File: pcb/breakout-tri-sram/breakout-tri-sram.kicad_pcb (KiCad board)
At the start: 4 copper layers, 100 x 100 mm, 148 parts, among them J101 FX18-120P-0.8SV20, J102 FX18-120S-0.8SV20, U101 IS61WV102416DBLL-10TLI, U102 IS61WV102416DBLL-10TLI, U103 IS61WV102416DBLL-10TLI, U201 74LCX541FT, U202 74LCX541FT, U203 74LCX541FT, U204 74LCX541FT, U205 74LCX541FT, U206 74LCX541FT, U207 74LCX541FT, U208 74LCX541FT, U209 74LCX541FT, U210 74LCX541FT, U211 74LCX541FT, U212 74LCX541FT, U301 74LCX541FT, U302 74LCX541FT, U303 74LCX541FT, U304 74LCX541FT, U305 74LCX541FT, U306 74LCX541FT, U401 74LCX541FT, U402 74LCX541FT, U403 74LCX541FT, U404 74LCX541FT, U405 74LCX541FT, U406 74LCX541FT, U501 74LCX541FT, U502 74LCX541FT, U503 74LCX541FT, U504 74LCX541FT, U505 74LCX541FT, U506 74LCX541FT, U507 74LCX541FT, U508 74LCX541FT, U509 74LCX541FT

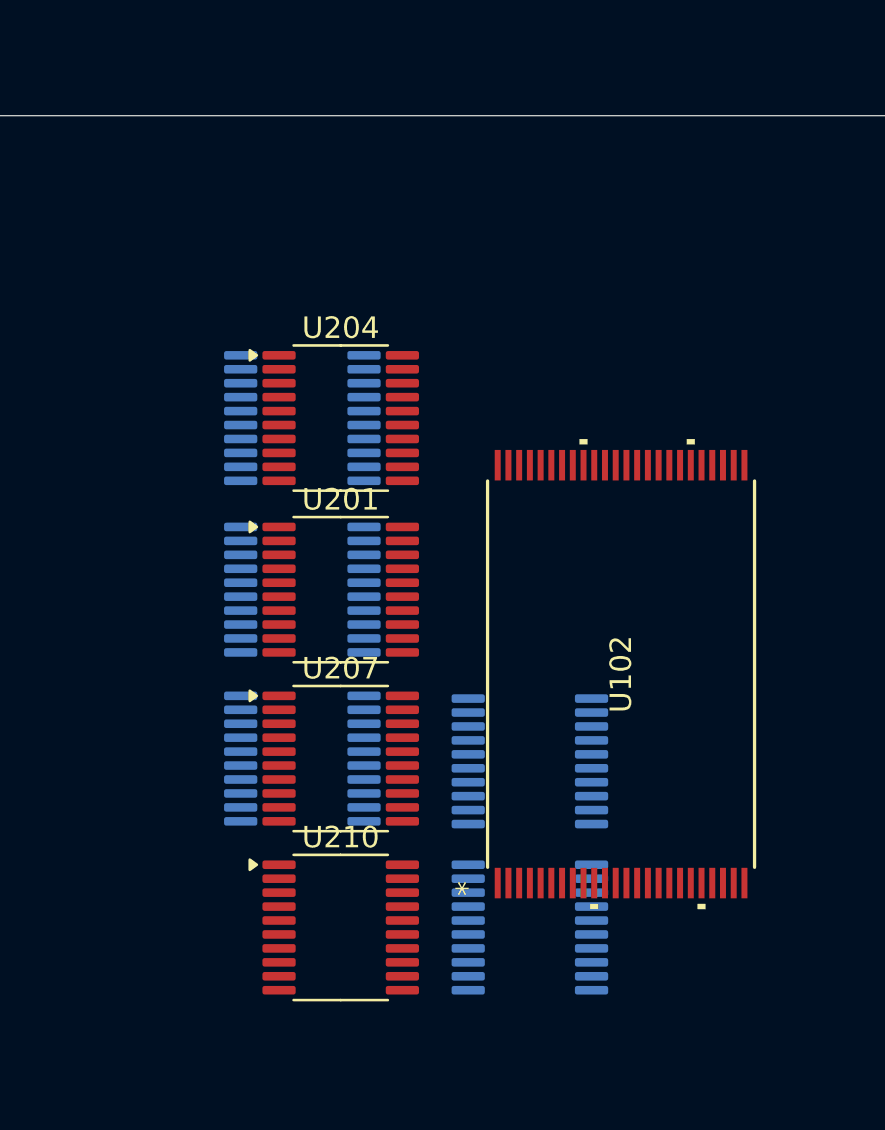
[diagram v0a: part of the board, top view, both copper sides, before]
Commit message: [pci][pci-sram] move to latched buffers
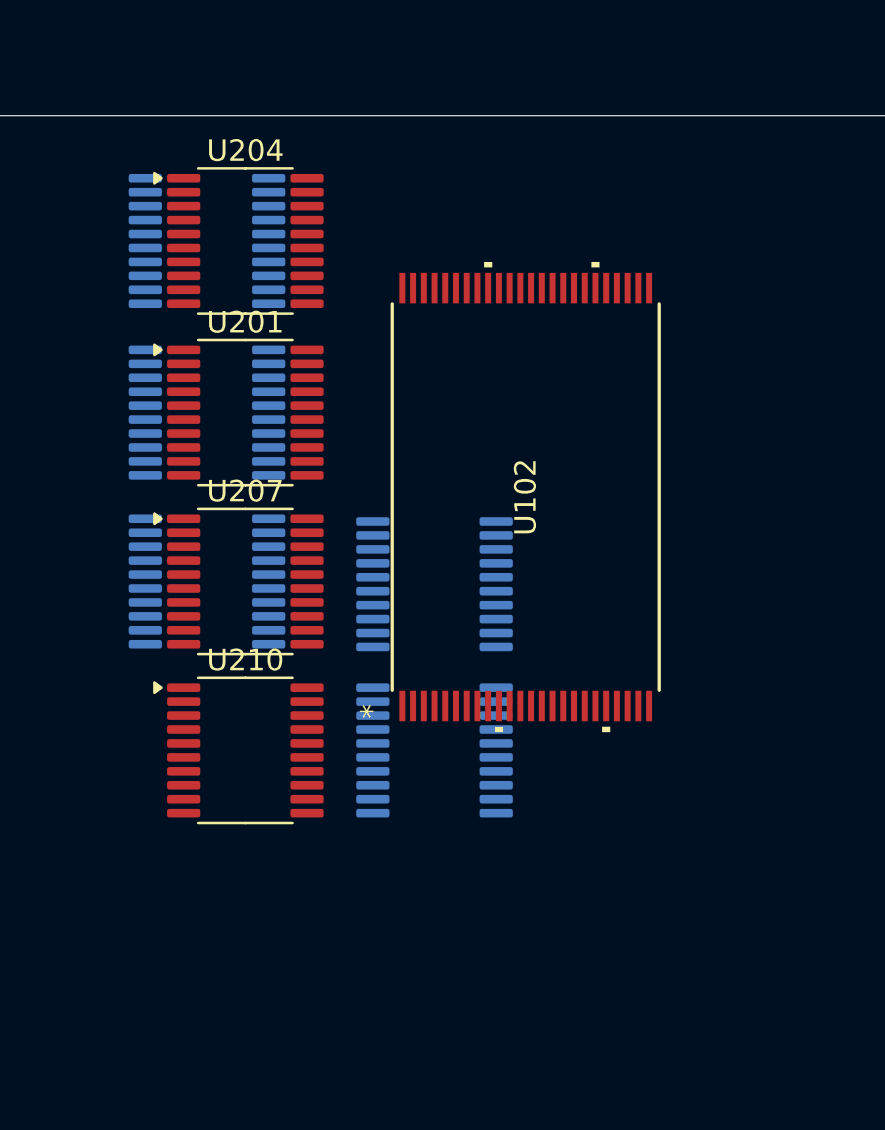
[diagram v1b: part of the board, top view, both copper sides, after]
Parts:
- U201, U202, U203, U204, U205, U206, U207, U208, U209, U210, U211, U212, U301, U302, U303, U304, U305, U306, U401, U402, U403, U404, U405, U406, U501, U502, U503, U504, U505, U506, U507, U508, U509: value 74LCX541FT -> 74LS573
- moved U102 9.38 mm to (53.2, 45.0)
- moved U201 9.38 mm to (40.1, 41.0)
- moved U210 9.38 mm to (40.1, 56.8)
- moved U301 9.38 mm to (49.0, 49.0)
- moved U304 9.38 mm to (49.0, 56.8)
- moved U501 9.38 mm to (38.4, 41.0)
- moved U204 9.38 mm to (40.1, 33.0)
- moved U207 9.38 mm to (40.1, 48.9)
- moved U504 9.38 mm to (38.4, 33.0)
- moved U507 9.38 mm to (38.4, 48.9)
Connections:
- J101 pad 51: unconnected-(J101-Pad51) -> /A2D_L
- J101 pad 52: unconnected-(J101-Pad52) -> /VGA_A_L
- J101 pad 53: unconnected-(J101-Pad53) -> /VGA_D_L
- U201 pad 11: /0_A7 -> /A2D_L
- U201 pad 12: /0_A6 -> /0_A7
- U201 pad 13: /0_A5 -> /0_A6
- U201 pad 14: /0_A4 -> /0_A5
- U201 pad 15: /0_A3 -> /0_A4
- U201 pad 16: /0_A2 -> /0_A3
- U201 pad 17: /0_A1 -> /0_A2
- U201 pad 18: /0_A0 -> /0_A1
- U201 pad 19: /A2D_0_EN# -> /0_A0
- U202 pad 11: /1_A7 -> /A2D_L
- U202 pad 12: /1_A6 -> /1_A7
- U202 pad 13: /1_A5 -> /1_A6
- U202 pad 14: /1_A4 -> /1_A5
- U202 pad 15: /1_A3 -> /1_A4
- U202 pad 16: /1_A2 -> /1_A3
- U202 pad 17: /1_A1 -> /1_A2
- U202 pad 18: /1_A0 -> /1_A1
- U202 pad 19: /A2D_1_EN# -> /1_A0
- U203 pad 11: /2_A7 -> /A2D_L
- U203 pad 12: /2_A6 -> /2_A7
- U203 pad 13: /2_A5 -> /2_A6
- U203 pad 14: /2_A4 -> /2_A5
- U203 pad 15: /2_A3 -> /2_A4
- U203 pad 16: /2_A2 -> /2_A3
- U203 pad 17: /2_A1 -> /2_A2
- U203 pad 18: /2_A0 -> /2_A1
- U203 pad 19: /A2D_2_EN# -> /2_A0
- U204 pad 11: /0_A15 -> /A2D_L
- U204 pad 12: /0_A14 -> /0_A15
- U204 pad 13: /0_A13 -> /0_A14
- U204 pad 14: /0_A12 -> /0_A13
- U204 pad 15: /0_A11 -> /0_A12
- U204 pad 16: /0_A10 -> /0_A11
- U204 pad 17: /0_A9 -> /0_A10
- U204 pad 18: /0_A8 -> /0_A9
- U204 pad 19: /A2D_0_EN# -> /0_A8
- U205 pad 11: /2_A15 -> /A2D_L
- U205 pad 12: /2_A14 -> /2_A15
- U205 pad 13: /2_A13 -> /2_A14
- U205 pad 14: /2_A12 -> /2_A13
- U205 pad 15: /2_A11 -> /2_A12
- U205 pad 16: /2_A10 -> /2_A11
- U205 pad 17: /2_A9 -> /2_A10
- U205 pad 18: /2_A8 -> /2_A9
- U205 pad 19: /A2D_2_EN# -> /2_A8
- U206 pad 11: /1_A15 -> /A2D_L
- U206 pad 12: /1_A14 -> /1_A15
- U206 pad 13: /1_A13 -> /1_A14
- U206 pad 14: /1_A12 -> /1_A13
- U206 pad 15: /1_A11 -> /1_A12
- U206 pad 16: /1_A10 -> /1_A11
- U206 pad 17: /1_A9 -> /1_A10
- U206 pad 18: /1_A8 -> /1_A9
- U206 pad 19: /A2D_1_EN# -> /1_A8
- U207 pad 11: /0_D3 -> /A2D_L
- U207 pad 12: /0_D2 -> /0_D3
- U207 pad 13: /0_D1 -> /0_D2
- U207 pad 14: /0_D0 -> /0_D1
- U207 pad 15: /0_A19 -> /0_D0
- U207 pad 16: /0_A18 -> /0_A19
- U207 pad 17: /0_A17 -> /0_A18
- U207 pad 18: /0_A16 -> /0_A17
- U207 pad 19: /A2D_0_EN# -> /0_A16
- U208 pad 11: /2_D3 -> /A2D_L
- U208 pad 12: /2_D2 -> /2_D3
- U208 pad 13: /2_D1 -> /2_D2
- U208 pad 14: /2_D0 -> /2_D1
- U208 pad 15: /2_A19 -> /2_D0
- U208 pad 16: /2_A18 -> /2_A19
- U208 pad 17: /2_A17 -> /2_A18
- U208 pad 18: /2_A16 -> /2_A17
- U208 pad 19: /A2D_2_EN# -> /2_A16
- U209 pad 11: /1_D3 -> /A2D_L
- U209 pad 12: /1_D2 -> /1_D3
- U209 pad 13: /1_D1 -> /1_D2
- U209 pad 14: /1_D0 -> /1_D1
- U209 pad 15: /1_A19 -> /1_D0
- U209 pad 16: /1_A18 -> /1_A19
- U209 pad 17: /1_A17 -> /1_A18
- U209 pad 18: /1_A16 -> /1_A17
- U209 pad 19: /A2D_1_EN# -> /1_A16
- U210 pad 11: /0_D11 -> /A2D_L
- U210 pad 12: /0_D10 -> /0_D11
- U210 pad 13: /0_D9 -> /0_D10
- U210 pad 14: /0_D8 -> /0_D9
- U210 pad 15: /0_D7 -> /0_D8
- U210 pad 16: /0_D6 -> /0_D7
- U210 pad 17: /0_D5 -> /0_D6
- U210 pad 18: /0_D4 -> /0_D5
- U210 pad 19: /A2D_0_EN# -> /0_D4
- U211 pad 11: /2_D11 -> /A2D_L
- U211 pad 12: /2_D10 -> /2_D11
- U211 pad 13: /2_D9 -> /2_D10
- U211 pad 14: /2_D8 -> /2_D9
- U211 pad 15: /2_D7 -> /2_D8
- U211 pad 16: /2_D6 -> /2_D7
- U211 pad 17: /2_D5 -> /2_D6
- U211 pad 18: /2_D4 -> /2_D5
- U211 pad 19: /A2D_2_EN# -> /2_D4
- U212 pad 11: /1_D11 -> /A2D_L
- U212 pad 12: /1_D10 -> /1_D11
- U212 pad 13: /1_D9 -> /1_D10
- U212 pad 14: /1_D8 -> /1_D9
- U212 pad 15: /1_D7 -> /1_D8
- U212 pad 16: /1_D6 -> /1_D7
- U212 pad 17: /1_D5 -> /1_D6
- U212 pad 18: /1_D4 -> /1_D5
- U212 pad 19: /A2D_1_EN# -> /1_D4
- U301 pad 11: /0_D3 -> +3V3
- U301 pad 12: /0_D2 -> /0_D3
- U301 pad 13: /0_D1 -> /0_D2
- U301 pad 14: /0_D0 -> /0_D1
- U301 pad 15: unconnected-(U301-Y3-Pad15) -> /0_D0
- U301 pad 19: /BLK_0_EN# -> unconnected-(U301-Q0-Pad19)
- U302 pad 11: /1_D3 -> +3V3
- U302 pad 12: /1_D2 -> /1_D3
- U302 pad 13: /1_D1 -> /1_D2
- U302 pad 14: /1_D0 -> /1_D1
- U302 pad 15: unconnected-(U302-Y3-Pad15) -> /1_D0
- U302 pad 19: /BLK_2_EN# -> unconnected-(U302-Q0-Pad19)
- U303 pad 11: /1_D3 -> +3V3
- U303 pad 12: /1_D2 -> /1_D3
- U303 pad 13: /1_D1 -> /1_D2
- U303 pad 14: /1_D0 -> /1_D1
- U303 pad 15: unconnected-(U303-Y3-Pad15) -> /1_D0
- U303 pad 19: /BLK_1_EN# -> unconnected-(U303-Q0-Pad19)
- U304 pad 11: /0_D11 -> +3V3
- U304 pad 12: /0_D10 -> /0_D11
- U304 pad 13: /0_D9 -> /0_D10
- U304 pad 14: /0_D8 -> /0_D9
- U304 pad 15: /0_D7 -> /0_D8
- U304 pad 16: /0_D6 -> /0_D7
- U304 pad 17: /0_D5 -> /0_D6
- U304 pad 18: /0_D4 -> /0_D5
- U304 pad 19: /BLK_0_EN# -> /0_D4
- U305 pad 11: /1_D11 -> +3V3
- U305 pad 12: /1_D10 -> /1_D11
- U305 pad 13: /1_D9 -> /1_D10
- U305 pad 14: /1_D8 -> /1_D9
- U305 pad 15: /1_D7 -> /1_D8
- U305 pad 16: /1_D6 -> /1_D7
- U305 pad 17: /1_D5 -> /1_D6
- U305 pad 18: /1_D4 -> /1_D5
- U305 pad 19: /BLK_2_EN# -> /1_D4
- U306 pad 11: /1_D11 -> +3V3
- U306 pad 12: /1_D10 -> /1_D11
- U306 pad 13: /1_D9 -> /1_D10
- U306 pad 14: /1_D8 -> /1_D9
- U306 pad 15: /1_D7 -> /1_D8
- U306 pad 16: /1_D6 -> /1_D7
- U306 pad 17: /1_D5 -> /1_D6
- U306 pad 18: /1_D4 -> /1_D5
- U306 pad 19: /BLK_1_EN# -> /1_D4
- U401 pad 11: /VGA_B_3 -> /VGA_D_L
- U401 pad 12: /VGA_B_2 -> /VGA_B_3
- U401 pad 13: /VGA_B_1 -> /VGA_B_2
- U401 pad 14: /VGA_B_0 -> /VGA_B_1
- U401 pad 15: unconnected-(U401-Y3-Pad15) -> /VGA_B_0
- U401 pad 17: /VGA_VSYNC -> unconnected-(U401-Q2-Pad17)
- U401 pad 18: /VGA_HSYNC -> /VGA_VSYNC
- U401 pad 19: /VGA_0_D_EN# -> /VGA_HSYNC
- U402 pad 11: /VGA_B_3 -> /VGA_D_L
- U402 pad 12: /VGA_B_2 -> /VGA_B_3
- U402 pad 13: /VGA_B_1 -> /VGA_B_2
- U402 pad 14: /VGA_B_0 -> /VGA_B_1
- U402 pad 15: unconnected-(U402-Y3-Pad15) -> /VGA_B_0
- U402 pad 17: /VGA_VSYNC -> unconnected-(U402-Q2-Pad17)
- U402 pad 18: /VGA_HSYNC -> /VGA_VSYNC
- U402 pad 19: /VGA_2_D_EN# -> /VGA_HSYNC
- U403 pad 11: /VGA_B_3 -> /VGA_D_L
- U403 pad 12: /VGA_B_2 -> /VGA_B_3
- U403 pad 13: /VGA_B_1 -> /VGA_B_2
- U403 pad 14: /VGA_B_0 -> /VGA_B_1
- U403 pad 15: unconnected-(U403-Y3-Pad15) -> /VGA_B_0
- U403 pad 17: /VGA_VSYNC -> unconnected-(U403-Q2-Pad17)
- U403 pad 18: /VGA_HSYNC -> /VGA_VSYNC
- U403 pad 19: /VGA_1_D_EN# -> /VGA_HSYNC
- U404 pad 11: /VGA_R_3 -> /VGA_D_L
- U404 pad 12: /VGA_R_2 -> /VGA_R_3
- U404 pad 13: /VGA_R_1 -> /VGA_R_2
- U404 pad 14: /VGA_R_0 -> /VGA_R_1
- U404 pad 15: /VGA_G_3 -> /VGA_R_0
- U404 pad 16: /VGA_G_2 -> /VGA_G_3
- U404 pad 17: /VGA_G_1 -> /VGA_G_2
- U404 pad 18: /VGA_G_0 -> /VGA_G_1
- U404 pad 19: /VGA_0_D_EN# -> /VGA_G_0
- U405 pad 11: /VGA_R_3 -> /VGA_D_L
- U405 pad 12: /VGA_R_2 -> /VGA_R_3
- U405 pad 13: /VGA_R_1 -> /VGA_R_2
- U405 pad 14: /VGA_R_0 -> /VGA_R_1
- U405 pad 15: /VGA_G_3 -> /VGA_R_0
- U405 pad 16: /VGA_G_2 -> /VGA_G_3
- U405 pad 17: /VGA_G_1 -> /VGA_G_2
- U405 pad 18: /VGA_G_0 -> /VGA_G_1
- U405 pad 19: /VGA_2_D_EN# -> /VGA_G_0
- U406 pad 11: /VGA_R_3 -> /VGA_D_L
- U406 pad 12: /VGA_R_2 -> /VGA_R_3
- U406 pad 13: /VGA_R_1 -> /VGA_R_2
- U406 pad 14: /VGA_R_0 -> /VGA_R_1
- U406 pad 15: /VGA_G_3 -> /VGA_R_0
- U406 pad 16: /VGA_G_2 -> /VGA_G_3
- U406 pad 17: /VGA_G_1 -> /VGA_G_2
- U406 pad 18: /VGA_G_0 -> /VGA_G_1
- U406 pad 19: /VGA_1_D_EN# -> /VGA_G_0
- U501 pad 11: /0_A7 -> /VGA_A_L
- U501 pad 12: /0_A6 -> /0_A7
- U501 pad 13: /0_A5 -> /0_A6
- U501 pad 14: /0_A4 -> /0_A5
- U501 pad 15: /0_A3 -> /0_A4
- U501 pad 16: /0_A2 -> /0_A3
- U501 pad 17: /0_A1 -> /0_A2
- U501 pad 18: /0_A0 -> /0_A1
- U501 pad 19: /VGA_0_A_EN# -> /0_A0
- U502 pad 11: /1_A7 -> /VGA_A_L
- U502 pad 12: /1_A6 -> /1_A7
- U502 pad 13: /1_A5 -> /1_A6
- U502 pad 14: /1_A4 -> /1_A5
- U502 pad 15: /1_A3 -> /1_A4
- U502 pad 16: /1_A2 -> /1_A3
- U502 pad 17: /1_A1 -> /1_A2
- U502 pad 18: /1_A0 -> /1_A1
- U502 pad 19: /VGA_1_A_EN# -> /1_A0
- U503 pad 11: /2_A7 -> /VGA_A_L
- U503 pad 12: /2_A6 -> /2_A7
- U503 pad 13: /2_A5 -> /2_A6
- U503 pad 14: /2_A4 -> /2_A5
- U503 pad 15: /2_A3 -> /2_A4
- U503 pad 16: /2_A2 -> /2_A3
- U503 pad 17: /2_A1 -> /2_A2
- U503 pad 18: /2_A0 -> /2_A1
- U503 pad 19: /VGA_2_A_EN# -> /2_A0
- U504 pad 11: /0_A15 -> /VGA_A_L
- U504 pad 12: /0_A14 -> /0_A15
- U504 pad 13: /0_A13 -> /0_A14
- U504 pad 14: /0_A12 -> /0_A13
- U504 pad 15: /0_A11 -> /0_A12
- U504 pad 16: /0_A10 -> /0_A11
- U504 pad 17: /0_A9 -> /0_A10
- U504 pad 18: /0_A8 -> /0_A9
- U504 pad 19: /VGA_0_A_EN# -> /0_A8
- U505 pad 11: /2_A15 -> /VGA_A_L
- U505 pad 12: /2_A14 -> /2_A15
- U505 pad 13: /2_A13 -> /2_A14
- U505 pad 14: /2_A12 -> /2_A13
- U505 pad 15: /2_A11 -> /2_A12
- U505 pad 16: /2_A10 -> /2_A11
- U505 pad 17: /2_A9 -> /2_A10
- U505 pad 18: /2_A8 -> /2_A9
- U505 pad 19: /VGA_2_A_EN# -> /2_A8
- U506 pad 11: /1_A15 -> /VGA_A_L
- U506 pad 12: /1_A14 -> /1_A15
- U506 pad 13: /1_A13 -> /1_A14
- U506 pad 14: /1_A12 -> /1_A13
- U506 pad 15: /1_A11 -> /1_A12
- U506 pad 16: /1_A10 -> /1_A11
- U506 pad 17: /1_A9 -> /1_A10
- U506 pad 18: /1_A8 -> /1_A9
- U506 pad 19: /VGA_1_A_EN# -> /1_A8
- U507 pad 11: unconnected-(U507-Y7-Pad11) -> /VGA_A_L
- U507 pad 15: /0_A19 -> unconnected-(U507-Q4-Pad15)
- U507 pad 16: /0_A18 -> /0_A19
- U507 pad 17: /0_A17 -> /0_A18
- U507 pad 18: /0_A16 -> /0_A17
- U507 pad 19: /VGA_0_A_EN# -> /0_A16
- U508 pad 11: unconnected-(U508-Y7-Pad11) -> /VGA_A_L
- U508 pad 15: /2_A19 -> unconnected-(U508-Q4-Pad15)
- U508 pad 16: /2_A18 -> /2_A19
- U508 pad 17: /2_A17 -> /2_A18
- U508 pad 18: /2_A16 -> /2_A17
- U508 pad 19: /VGA_2_A_EN# -> /2_A16
- U509 pad 11: unconnected-(U509-Y7-Pad11) -> /VGA_A_L
- U509 pad 15: /1_A19 -> unconnected-(U509-Q4-Pad15)
- U509 pad 16: /1_A18 -> /1_A19
- U509 pad 17: /1_A17 -> /1_A18
- U509 pad 18: /1_A16 -> /1_A17
- U509 pad 19: /VGA_1_A_EN# -> /1_A16

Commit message: [pcb][tri-sram] 3xsram routed
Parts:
- removed C202, C205, C208, C211, C214, C217, C220, C223, C226, C229, C232, C235, C302, C305, C308, C311, C314, C317, C402, C405, C408, C411, C414, C502, C505, C508, C511, C514, C517, C520, C523, C526: 0.1uf, Capacitor_SMD:C_0402_1005Metric
- removed C210, C213, C216, C219, C222, C225, C228, C231, C234, C301, C304, C307, C310, C313, C316, C401, C404, C407, C416, C501, C504, C507, C510, C513, C516: 22uf, Capacitor_SMD:C_0603_1608Metric
- C303, C306, C309, C312, C315, C318, C403, C406, C409, C410, C412, C413, C415, C417, C418, C503, C506, C509, C512, C515, C518, C519, C521, C522, C524, C525, C527, U302, U303, U305, U306, U401, U402, U403, U404, U405, U406, U502, U503, U505, U506, U508, U509: moved to B.Cu
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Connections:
- U201 pad 12: /0_A7 -> /0_A0
- U201 pad 13: /0_A6 -> /0_A19
- U201 pad 14: /0_A5 -> /0_A18
- U201 pad 15: /0_A4 -> /0_A17
- U201 pad 16: /0_A3 -> /0_A16
- U201 pad 17: /0_A2 -> /0_A15
- U201 pad 18: /0_A1 -> /0_A6
- U201 pad 19: /0_A0 -> /0_A5
- U201 pad 2: /A2D_X_0 -> /A2D_X_5
- U201 pad 3: /A2D_X_1 -> /A2D_X_6
- U201 pad 4: /A2D_X_2 -> /A2D_Y_5
- U201 pad 5: /A2D_X_3 -> /A2D_Y_6
- U201 pad 6: /A2D_X_4 -> /A2D_Y_7
- U201 pad 7: /A2D_X_5 -> /A2D_Y_8
- U201 pad 8: /A2D_X_6 -> /A2D_Y_9
- U201 pad 9: /A2D_X_7 -> /A2D_X_0
- U202 pad 12: /1_A7 -> /1_A0
- U202 pad 13: /1_A6 -> /1_A19
- U202 pad 14: /1_A5 -> /1_A18
- U202 pad 15: /1_A4 -> /1_A17
- U202 pad 16: /1_A3 -> /1_A16
- U202 pad 17: /1_A2 -> /1_A15
- U202 pad 18: /1_A1 -> /1_A6
- U202 pad 19: /1_A0 -> /1_A5
- U202 pad 2: /A2D_X_0 -> /A2D_X_5
- U202 pad 3: /A2D_X_1 -> /A2D_X_6
- U202 pad 4: /A2D_X_2 -> /A2D_Y_5
- U202 pad 5: /A2D_X_3 -> /A2D_Y_6
- U202 pad 6: /A2D_X_4 -> /A2D_Y_7
- U202 pad 7: /A2D_X_5 -> /A2D_Y_8
- U202 pad 8: /A2D_X_6 -> /A2D_Y_9
- U202 pad 9: /A2D_X_7 -> /A2D_X_0
- U203 pad 12: /2_A7 -> /2_A0
- U203 pad 13: /2_A6 -> /2_A19
- U203 pad 14: /2_A5 -> /2_A18
- U203 pad 15: /2_A4 -> /2_A17
- U203 pad 16: /2_A3 -> /2_A16
- U203 pad 17: /2_A2 -> /2_A15
- U203 pad 18: /2_A1 -> /2_A6
- U203 pad 19: /2_A0 -> /2_A5
- U203 pad 2: /A2D_X_0 -> /A2D_X_5
- U203 pad 3: /A2D_X_1 -> /A2D_X_6
- U203 pad 4: /A2D_X_2 -> /A2D_Y_5
- U203 pad 5: /A2D_X_3 -> /A2D_Y_6
- U203 pad 6: /A2D_X_4 -> /A2D_Y_7
- U203 pad 7: /A2D_X_5 -> /A2D_Y_8
- U203 pad 8: /A2D_X_6 -> /A2D_Y_9
- U203 pad 9: /A2D_X_7 -> /A2D_X_0
- U204 pad 12: /0_A15 -> /0_A7
- U204 pad 13: /0_A14 -> /0_A8
- U204 pad 14: /0_A13 -> /0_A9
- U204 pad 15: /0_A12 -> /0_A10
- U204 pad 17: /0_A10 -> /0_A12
- U204 pad 18: /0_A9 -> /0_A13
- U204 pad 19: /0_A8 -> /0_A14
- U204 pad 2: /A2D_X_8 -> /A2D_Y_4
- U204 pad 3: /A2D_X_9 -> /A2D_Y_3
- U204 pad 4: /A2D_Y_0 -> /A2D_Y_2
- U204 pad 6: /A2D_Y_2 -> /A2D_Y_0
- U204 pad 7: /A2D_Y_3 -> /A2D_X_9
- U204 pad 8: /A2D_Y_4 -> /A2D_X_8
- U204 pad 9: /A2D_Y_5 -> /A2D_X_7
- U205 pad 12: /2_A15 -> /2_A7
- U205 pad 13: /2_A14 -> /2_A8
- U205 pad 14: /2_A13 -> /2_A9
- U205 pad 15: /2_A12 -> /2_A10
- U205 pad 17: /2_A10 -> /2_A12
- U205 pad 18: /2_A9 -> /2_A13
- U205 pad 19: /2_A8 -> /2_A14
- U205 pad 2: /A2D_X_8 -> /A2D_Y_4
- U205 pad 3: /A2D_X_9 -> /A2D_Y_3
- U205 pad 4: /A2D_Y_0 -> /A2D_Y_2
- U205 pad 6: /A2D_Y_2 -> /A2D_Y_0
- U205 pad 7: /A2D_Y_3 -> /A2D_X_9
- U205 pad 8: /A2D_Y_4 -> /A2D_X_8
- U205 pad 9: /A2D_Y_5 -> /A2D_X_7
- U206 pad 12: /1_A15 -> /1_A7
- U206 pad 13: /1_A14 -> /1_A8
- U206 pad 14: /1_A13 -> /1_A9
- U206 pad 15: /1_A12 -> /1_A10
- U206 pad 17: /1_A10 -> /1_A12
- U206 pad 18: /1_A9 -> /1_A13
- U206 pad 19: /1_A8 -> /1_A14
- U206 pad 2: /A2D_X_8 -> /A2D_Y_4
- U206 pad 3: /A2D_X_9 -> /A2D_Y_3
- U206 pad 4: /A2D_Y_0 -> /A2D_Y_2
- U206 pad 6: /A2D_Y_2 -> /A2D_Y_0
- U206 pad 7: /A2D_Y_3 -> /A2D_X_9
- U206 pad 8: /A2D_Y_4 -> /A2D_X_8
- U206 pad 9: /A2D_Y_5 -> /A2D_X_7
- U207 pad 12: /0_D3 -> /0_D0
- U207 pad 13: /0_D2 -> /0_D1
- U207 pad 14: /0_D1 -> /0_D2
- U207 pad 15: /0_D0 -> /0_D3
- U207 pad 16: /0_A19 -> /0_A4
- U207 pad 17: /0_A18 -> /0_A3
- U207 pad 18: /0_A17 -> /0_A2
- U207 pad 19: /0_A16 -> /0_A1
- U207 pad 2: /A2D_Y_6 -> /A2D_X_1
- U207 pad 3: /A2D_Y_7 -> /A2D_X_2
- U207 pad 4: /A2D_Y_8 -> /A2D_X_3
- U207 pad 5: /A2D_Y_9 -> /A2D_X_4
- U207 pad 6: /A2D_B_0 -> /A2D_B_3
- U207 pad 7: /A2D_B_1 -> /A2D_B_2
- U207 pad 8: /A2D_B_2 -> /A2D_B_1
- U207 pad 9: /A2D_B_3 -> /A2D_B_0
- U208 pad 12: /2_D3 -> /2_D0
- U208 pad 13: /2_D2 -> /2_D1
- U208 pad 14: /2_D1 -> /2_D2
- U208 pad 15: /2_D0 -> /2_D3
- U208 pad 16: /2_A19 -> /2_A4
- U208 pad 17: /2_A18 -> /2_A3
- U208 pad 18: /2_A17 -> /2_A2
- U208 pad 19: /2_A16 -> /2_A1
- U208 pad 2: /A2D_Y_6 -> /A2D_X_1
- U208 pad 3: /A2D_Y_7 -> /A2D_X_2
- U208 pad 4: /A2D_Y_8 -> /A2D_X_3
- U208 pad 5: /A2D_Y_9 -> /A2D_X_4
- U208 pad 6: /A2D_B_0 -> /A2D_B_3
- U208 pad 7: /A2D_B_1 -> /A2D_B_2
- U208 pad 8: /A2D_B_2 -> /A2D_B_1
- U208 pad 9: /A2D_B_3 -> /A2D_B_0
- U209 pad 12: /1_D3 -> /1_D0
- U209 pad 13: /1_D2 -> /1_D1
- U209 pad 14: /1_D1 -> /1_D2
- U209 pad 15: /1_D0 -> /1_D3
- U209 pad 16: /1_A19 -> /1_A4
- U209 pad 17: /1_A18 -> /1_A3
- U209 pad 18: /1_A17 -> /1_A2
- U209 pad 19: /1_A16 -> /1_A1
- U209 pad 2: /A2D_Y_6 -> /A2D_X_1
- U209 pad 3: /A2D_Y_7 -> /A2D_X_2
- U209 pad 4: /A2D_Y_8 -> /A2D_X_3
- U209 pad 5: /A2D_Y_9 -> /A2D_X_4
- U209 pad 6: /A2D_B_0 -> /A2D_B_3
- U209 pad 7: /A2D_B_1 -> /A2D_B_2
- U209 pad 8: /A2D_B_2 -> /A2D_B_1
- U209 pad 9: /A2D_B_3 -> /A2D_B_0
- U210 pad 12: /0_D11 -> /0_D8
- U210 pad 13: /0_D10 -> /0_D9
- U210 pad 14: /0_D9 -> /0_D10
- U210 pad 15: /0_D8 -> /0_D11
- U210 pad 6: /A2D_R_0 -> /A2D_R_3
- U210 pad 7: /A2D_R_1 -> /A2D_R_2
- U210 pad 8: /A2D_R_2 -> /A2D_R_1
- U210 pad 9: /A2D_R_3 -> /A2D_R_0
- U211 pad 12: /2_D11 -> /2_D8
- U211 pad 13: /2_D10 -> /2_D9
- U211 pad 14: /2_D9 -> /2_D10
- U211 pad 15: /2_D8 -> /2_D11
- U211 pad 6: /A2D_R_0 -> /A2D_R_3
- U211 pad 7: /A2D_R_1 -> /A2D_R_2
- U211 pad 8: /A2D_R_2 -> /A2D_R_1
- U211 pad 9: /A2D_R_3 -> /A2D_R_0
- U212 pad 12: /1_D11 -> /1_D8
- U212 pad 13: /1_D10 -> /1_D9
- U212 pad 14: /1_D9 -> /1_D10
- U212 pad 15: /1_D8 -> /1_D11
- U212 pad 6: /A2D_R_0 -> /A2D_R_3
- U212 pad 7: /A2D_R_1 -> /A2D_R_2
- U212 pad 8: /A2D_R_2 -> /A2D_R_1
- U212 pad 9: /A2D_R_3 -> /A2D_R_0
- U301 pad 12: /0_D3 -> /0_D0
- U301 pad 13: /0_D2 -> /0_D1
- U301 pad 14: /0_D1 -> /0_D2
- U301 pad 15: /0_D0 -> /0_D3
- U302 pad 12: /1_D3 -> /2_D0
- U302 pad 13: /1_D2 -> /2_D1
- U302 pad 14: /1_D1 -> /2_D2
- U302 pad 15: /1_D0 -> /2_D3
- U303 pad 12: /1_D3 -> /1_D0
- U303 pad 13: /1_D2 -> /1_D1
- U303 pad 14: /1_D1 -> /1_D2
- U303 pad 15: /1_D0 -> /1_D3
- U304 pad 12: /0_D11 -> /0_D9
- U304 pad 14: /0_D9 -> /0_D11
- U305 pad 12: /1_D11 -> /2_D9
- U305 pad 13: /1_D10 -> /2_D10
- U305 pad 14: /1_D9 -> /2_D11
- U305 pad 15: /1_D8 -> /2_D8
- U305 pad 16: /1_D7 -> /2_D7
- U305 pad 17: /1_D6 -> /2_D6
- U305 pad 18: /1_D5 -> /2_D5
- U305 pad 19: /1_D4 -> /2_D4
- U306 pad 12: /1_D11 -> /1_D9
- U306 pad 14: /1_D9 -> /1_D11
- U401 pad 12: /VGA_B_3 -> /VGA_R_3
- U401 pad 13: /VGA_B_2 -> /VGA_R_2
- U401 pad 14: /VGA_B_1 -> /VGA_R_1
- U401 pad 15: /VGA_B_0 -> /VGA_R_0
- U401 pad 6: /0_D0 -> /0_D8
- U401 pad 7: /0_D1 -> /0_D9
- U401 pad 8: /0_D2 -> /0_D10
- U401 pad 9: /0_D3 -> /0_D11
- U402 pad 12: /VGA_B_3 -> /VGA_R_3
- U402 pad 13: /VGA_B_2 -> /VGA_R_2
- U402 pad 14: /VGA_B_1 -> /VGA_R_1
- U402 pad 15: /VGA_B_0 -> /VGA_R_0
- U402 pad 6: /2_D0 -> /2_D8
- U402 pad 7: /2_D1 -> /2_D9
- U402 pad 8: /2_D2 -> /2_D10
- U402 pad 9: /2_D3 -> /2_D11
- U403 pad 12: /VGA_B_3 -> /VGA_R_3
- U403 pad 13: /VGA_B_2 -> /VGA_R_2
- U403 pad 14: /VGA_B_1 -> /VGA_R_1
- U403 pad 15: /VGA_B_0 -> /VGA_R_0
- U403 pad 6: /1_D0 -> /1_D8
- U403 pad 7: /1_D1 -> /1_D9
- U403 pad 8: /1_D2 -> /1_D10
- U403 pad 9: /1_D3 -> /1_D11
- U404 pad 12: /VGA_R_3 -> /VGA_B_3
- U404 pad 13: /VGA_R_2 -> /VGA_B_2
- U404 pad 14: /VGA_R_1 -> /VGA_B_1
- U404 pad 15: /VGA_R_0 -> /VGA_B_0
- U404 pad 16: /VGA_G_3 -> /VGA_G_0
- U404 pad 17: /VGA_G_2 -> /VGA_G_1
- U404 pad 18: /VGA_G_1 -> /VGA_G_2
- U404 pad 19: /VGA_G_0 -> /VGA_G_3
- U404 pad 2: /0_D4 -> /0_D7
- U404 pad 3: /0_D5 -> /0_D6
- U404 pad 4: /0_D6 -> /0_D5
- U404 pad 5: /0_D7 -> /0_D4
- U404 pad 6: /0_D8 -> /0_D0
- U404 pad 7: /0_D9 -> /0_D1
- U404 pad 8: /0_D10 -> /0_D2
- U404 pad 9: /0_D11 -> /0_D3
- U405 pad 12: /VGA_R_3 -> /VGA_B_3
- U405 pad 13: /VGA_R_2 -> /VGA_B_2
- U405 pad 14: /VGA_R_1 -> /VGA_B_1
- U405 pad 15: /VGA_R_0 -> /VGA_B_0
- U405 pad 16: /VGA_G_3 -> /VGA_G_0
- U405 pad 17: /VGA_G_2 -> /VGA_G_1
- U405 pad 18: /VGA_G_1 -> /VGA_G_2
- U405 pad 19: /VGA_G_0 -> /VGA_G_3
- U405 pad 2: /2_D4 -> /2_D7
- U405 pad 3: /2_D5 -> /2_D6
- U405 pad 4: /2_D6 -> /2_D5
- U405 pad 5: /2_D7 -> /2_D4
- U405 pad 6: /2_D8 -> /2_D0
- U405 pad 7: /2_D9 -> /2_D1
- U405 pad 8: /2_D10 -> /2_D2
- U405 pad 9: /2_D11 -> /2_D3
- U406 pad 12: /VGA_R_3 -> /VGA_B_3
- U406 pad 13: /VGA_R_2 -> /VGA_B_2
- U406 pad 14: /VGA_R_1 -> /VGA_B_1
- U406 pad 15: /VGA_R_0 -> /VGA_B_0
- U406 pad 16: /VGA_G_3 -> /VGA_G_0
- U406 pad 17: /VGA_G_2 -> /VGA_G_1
- U406 pad 18: /VGA_G_1 -> /VGA_G_2
- U406 pad 19: /VGA_G_0 -> /VGA_G_3
- U406 pad 2: /1_D4 -> /1_D7
- U406 pad 3: /1_D5 -> /1_D6
- U406 pad 4: /1_D6 -> /1_D5
- U406 pad 5: /1_D7 -> /1_D4
- U406 pad 6: /1_D8 -> /1_D0
- U406 pad 7: /1_D9 -> /1_D1
- U406 pad 8: /1_D10 -> /1_D2
- U406 pad 9: /1_D11 -> /1_D3
- U501 pad 12: /0_A7 -> /0_A5
- U501 pad 14: /0_A5 -> /0_A15
- U501 pad 15: /0_A4 -> /0_A16
- U501 pad 16: /0_A3 -> /0_A17
- U501 pad 17: /0_A2 -> /0_A18
- U501 pad 18: /0_A1 -> /0_A19
- U501 pad 3: /VGA_A1 -> /VGA_A19
- U501 pad 4: /VGA_A2 -> /VGA_A18
- U501 pad 5: /VGA_A3 -> /VGA_A17
- U501 pad 6: /VGA_A4 -> /VGA_A16
- U501 pad 7: /VGA_A5 -> /VGA_A15
- U501 pad 9: /VGA_A7 -> /VGA_A5
- U502 pad 12: /1_A7 -> /1_A5
- U502 pad 14: /1_A5 -> /1_A15
- U502 pad 15: /1_A4 -> /1_A16
- U502 pad 16: /1_A3 -> /1_A17
- U502 pad 17: /1_A2 -> /1_A18
- U502 pad 18: /1_A1 -> /1_A19
- U502 pad 3: /VGA_A1 -> /VGA_A19
- U502 pad 4: /VGA_A2 -> /VGA_A18
- U502 pad 5: /VGA_A3 -> /VGA_A17
- U502 pad 6: /VGA_A4 -> /VGA_A16
- U502 pad 7: /VGA_A5 -> /VGA_A15
- U502 pad 9: /VGA_A7 -> /VGA_A5
- U503 pad 12: /2_A7 -> /2_A5
- U503 pad 14: /2_A5 -> /2_A15
- U503 pad 15: /2_A4 -> /2_A16
- U503 pad 16: /2_A3 -> /2_A17
- U503 pad 17: /2_A2 -> /2_A18
- U503 pad 18: /2_A1 -> /2_A19
- U503 pad 3: /VGA_A1 -> /VGA_A19
- U503 pad 4: /VGA_A2 -> /VGA_A18
- U503 pad 5: /VGA_A3 -> /VGA_A17
- U503 pad 6: /VGA_A4 -> /VGA_A16
- U503 pad 7: /VGA_A5 -> /VGA_A15
- U503 pad 9: /VGA_A7 -> /VGA_A5
- U504 pad 12: /0_A15 -> /0_A14
- U504 pad 13: /0_A14 -> /0_A13
- U504 pad 14: /0_A13 -> /0_A12
- U504 pad 15: /0_A12 -> /0_A11
- U504 pad 16: /0_A11 -> /0_A10
- U504 pad 17: /0_A10 -> /0_A9
- U504 pad 18: /0_A9 -> /0_A8
- U504 pad 19: /0_A8 -> /0_A7
- U504 pad 2: /VGA_A8 -> /VGA_A7
- U504 pad 3: /VGA_A9 -> /VGA_A8
- U504 pad 4: /VGA_A10 -> /VGA_A9
- U504 pad 5: /VGA_A11 -> /VGA_A10
- U504 pad 6: /VGA_A12 -> /VGA_A11
- U504 pad 7: /VGA_A13 -> /VGA_A12
- U504 pad 8: /VGA_A14 -> /VGA_A13
- U504 pad 9: /VGA_A15 -> /VGA_A14
- U505 pad 12: /2_A15 -> /2_A14
- U505 pad 13: /2_A14 -> /2_A13
- U505 pad 14: /2_A13 -> /2_A12
- U505 pad 15: /2_A12 -> /2_A11
- U505 pad 16: /2_A11 -> /2_A10
- U505 pad 17: /2_A10 -> /2_A9
- U505 pad 18: /2_A9 -> /2_A8
- U505 pad 19: /2_A8 -> /2_A7
- U506 pad 12: /1_A15 -> /1_A14
- U506 pad 13: /1_A14 -> /1_A13
- U506 pad 14: /1_A13 -> /1_A12
- U506 pad 15: /1_A12 -> /1_A11
- U506 pad 16: /1_A11 -> /1_A10
- U506 pad 17: /1_A10 -> /1_A9
- U506 pad 18: /1_A9 -> /1_A8
- U506 pad 19: /1_A8 -> /1_A7
- U506 pad 2: /VGA_A8 -> /VGA_A7
- U506 pad 3: /VGA_A9 -> /VGA_A8
- U506 pad 4: /VGA_A10 -> /VGA_A9
- U506 pad 5: /VGA_A11 -> /VGA_A10
- U506 pad 6: /VGA_A12 -> /VGA_A11
- U506 pad 7: /VGA_A13 -> /VGA_A12
- U506 pad 8: /VGA_A14 -> /VGA_A13
- U506 pad 9: /VGA_A15 -> /VGA_A14
- U507 pad 12: unconnected-(U507-Q7-Pad12) -> /0_A1
- U507 pad 13: unconnected-(U507-Q6-Pad13) -> /0_A2
- U507 pad 14: unconnected-(U507-Q5-Pad14) -> /0_A3
- U507 pad 15: unconnected-(U507-Q4-Pad15) -> /0_A4
- U507 pad 16: /0_A19 -> unconnected-(U507-Q3-Pad16)
- U507 pad 17: /0_A18 -> unconnected-(U507-Q2-Pad17)
- U507 pad 18: /0_A17 -> unconnected-(U507-Q1-Pad18)
- U507 pad 19: /0_A16 -> unconnected-(U507-Q0-Pad19)
- U507 pad 2: /VGA_A16 -> unconnected-(U507-D0-Pad2)
- U507 pad 3: /VGA_A17 -> unconnected-(U507-D1-Pad3)
- U507 pad 4: /VGA_A18 -> unconnected-(U507-D2-Pad4)
- U507 pad 5: /VGA_A19 -> unconnected-(U507-D3-Pad5)
- U507 pad 6: unconnected-(U507-D4-Pad6) -> /VGA_A4
- U507 pad 7: unconnected-(U507-D5-Pad7) -> /VGA_A3
- U507 pad 8: unconnected-(U507-D6-Pad8) -> /VGA_A2
- U507 pad 9: unconnected-(U507-D7-Pad9) -> /VGA_A1
- U508 pad 12: unconnected-(U508-Q7-Pad12) -> /2_A1
- U508 pad 13: unconnected-(U508-Q6-Pad13) -> /2_A2
- U508 pad 14: unconnected-(U508-Q5-Pad14) -> /2_A3
- U508 pad 15: unconnected-(U508-Q4-Pad15) -> /2_A4
- U508 pad 16: /2_A19 -> unconnected-(U508-Q3-Pad16)
- U508 pad 17: /2_A18 -> unconnected-(U508-Q2-Pad17)
- U508 pad 18: /2_A17 -> unconnected-(U508-Q1-Pad18)
- U508 pad 19: /2_A16 -> unconnected-(U508-Q0-Pad19)
- U508 pad 2: /VGA_A16 -> unconnected-(U508-D0-Pad2)
- U508 pad 3: /VGA_A17 -> unconnected-(U508-D1-Pad3)
- U508 pad 4: /VGA_A18 -> unconnected-(U508-D2-Pad4)
- U508 pad 5: /VGA_A19 -> unconnected-(U508-D3-Pad5)
- U508 pad 6: unconnected-(U508-D4-Pad6) -> /VGA_A4
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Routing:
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
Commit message: [pcb][tri-sram] tri-sram complete
squashed big-bus branch
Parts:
- removed C218, C221, C224, C227, C230, C233, C236, C315, C318, C412, C415, C417, C418, C509, C512, C515, C518, C521, C524, C527: 0.1uf, Capacitor_SMD:C_0402_1005Metric
- removed C410, C413, C519, C522, C525: 22uf, Capacitor_SMD:C_0603_1608Metric
- removed U507, U508, U509: 74LS573, Package_SO:SSOP-20_4.4x6.5mm_P0.65mm
- added C110: 0.1uf, Capacitor_SMD:C_0402_1005Metric, F.Cu at (223.4, 121.7)
- added C202: 0.1uf, Capacitor_SMD:C_0402_1005Metric, F.Cu at (110.6, 123.1)
- added C205: 0.1uf, Capacitor_SMD:C_0402_1005Metric, F.Cu at (126.3, 118.9)
- added C208: 0.1uf, Capacitor_SMD:C_0402_1005Metric, F.Cu at (174.8, 93.8)
- added C210: 0.1uf, Capacitor_SMD:C_0402_1005Metric, F.Cu at (178.7, 118.9)
- added C211: 22uf, Capacitor_SMD:C_0603_1608Metric, F.Cu at (231.0, 121.0)
- added C213: 0.1uf, Capacitor_SMD:C_0402_1005Metric, F.Cu at (227.4, 93.8)
- added C214: 0.1uf, Capacitor_SMD:C_0402_1005Metric, F.Cu at (215.9, 105.1)
- added C301: 22uf, Capacitor_SMD:C_0603_1608Metric, F.Cu at (132.7, 94.2)
- added C302: 0.1uf, Capacitor_SMD:C_0402_1005Metric, F.Cu at (119.3, 123.2)
- added C304: 0.1uf, Capacitor_SMD:C_0402_1005Metric, F.Cu at (110.8, 114.4)
- added C305: 22uf, Capacitor_SMD:C_0603_1608Metric, F.Cu at (185.1, 94.2)
- added C307: 0.1uf, Capacitor_SMD:C_0402_1005Metric, F.Cu at (183.2, 93.8)
- added C308: 0.1uf, Capacitor_SMD:C_0402_1005Metric, F.Cu at (163.2, 114.4)
- added C310: 0.1uf, Capacitor_SMD:C_0402_1005Metric, F.Cu at (224.3, 123.2)
- added C311: 0.1uf, Capacitor_SMD:C_0402_1005Metric, F.Cu at (235.8, 93.8)
- added C401: 22uf, Capacitor_SMD:C_0603_1608Metric, F.Cu at (132.3, 99.8)
- added C402: 0.1uf, Capacitor_SMD:C_0402_1005Metric, F.Cu at (105.7, 87.2)
- added C404: 22uf, Capacitor_SMD:C_0603_1608Metric, F.Cu at (184.6, 99.8)
- added C405: 0.1uf, Capacitor_SMD:C_0402_1005Metric, F.Cu at (158.0, 87.2)
- added C407: 22uf, Capacitor_SMD:C_0603_1608Metric, F.Cu at (237.3, 99.8)
- added C408: 0.1uf, Capacitor_SMD:C_0402_1005Metric, F.Cu at (210.7, 87.2)
- added C501: 0.1uf, Capacitor_SMD:C_0402_1005Metric, F.Cu at (108.5, 95.6)
- added C502: 0.1uf, Capacitor_SMD:C_0402_1005Metric, F.Cu at (127.3, 123.2)
- added C504: 0.1uf, Capacitor_SMD:C_0402_1005Metric, F.Cu at (179.7, 123.2)
- added C505: 0.1uf, Capacitor_SMD:C_0402_1005Metric, F.Cu at (213.5, 95.6)
- added PM103: Conn_02x06_Top_Bottom, custom:PMOD_12p_Horizontal, F.Cu at (64.6, 137.2)
- added U104: IS61WV102416DBLL-10TLI, footprints:IS61WV102416DBLL-10TLI_ISI, F.Cu at (223.2, 109.7)
- added U307: 74LS573, Package_SO:SSOP-20_4.4x6.5mm_P0.65mm, F.Cu at (227.7, 127.9)
- added U308: 74LS573, Package_SO:SSOP-20_4.4x6.5mm_P0.65mm, F.Cu at (231.6, 90.2)
- added U309: 74LS573, Package_SO:SSOP-20_4.4x6.5mm_P0.65mm, F.Cu at (210.9, 116.9)
- C101, C104, C107, C204, C207: value 22uf -> 0.1uf; footprint Capacitor_SMD:C_0603_1608Metric -> Capacitor_SMD:C_0402_1005Metric
- C102, C105, C108, C206: value 0.1uf -> 22uf; footprint Capacitor_SMD:C_0402_1005Metric -> Capacitor_SMD:C_0603_1608Metric
- C303, C306, C312, C403, C406, C409, C503, C506, U301, U302, U303, U304, U305, U306, U401, U402, U403, U404, U405, U406, U501, U502, U503, U504, U505, U506: moved to F.Cu
- C309: value 0.1uf -> 22uf; footprint Capacitor_SMD:C_0402_1005Metric -> Capacitor_SMD:C_0603_1608Metric; moved to F.Cu
- U101: value IS61WV102416DBLL-10TLI -> 74LS573; footprint footprints:IS61WV102416DBLL-10TLI_ISI -> Package_SO:SSOP-20_4.4x6.5mm_P0.65mm
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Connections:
- J101 pad 10: /VGA_1_A_EN# -> /VGA_A7
- J101 pad 111: unconnected-(J101-Pad111) -> /LK_01
- J101 pad 112: unconnected-(J101-Pad112) -> /LK_05
- J101 pad 113: unconnected-(J101-Pad113) -> /LK_02
- J101 pad 114: unconnected-(J101-Pad114) -> /LK_06
- J101 pad 115: unconnected-(J101-Pad115) -> /LK_03
- J101 pad 116: unconnected-(J101-Pad116) -> /LK_07
- J101 pad 117: unconnected-(J101-Pad117) -> /LK_04
- J101 pad 118: unconnected-(J101-Pad118) -> /LK_08
- J101 pad 13: /VGA_2_A_EN# -> /VGA_D_L
- J101 pad 14: /HSYNC -> /BLK_2_EN#
- J101 pad 15: /VSYNC -> /VGA_2_D_EN#
- J101 pad 16: /VGA_A0 -> /BLK_1_EN#
- J101 pad 17: /VGA_A1 -> /VGA_1_D_EN#
- J101 pad 18: /VGA_A2 -> /BLK_0_EN#
- J101 pad 19: /VGA_A3 -> /VGA_0_D_EN#
- J101 pad 20: /VGA_A4 -> unconnected-(J101-Pad20)
- J101 pad 23: /VGA_A5 -> /HSYNC
- J101 pad 24: /VGA_A6 -> /VSYNC
- J101 pad 25: /VGA_A7 -> /2_OE#
- J101 pad 26: /VGA_A8 -> /1_OE#
- J101 pad 27: /VGA_A9 -> /0_OE#
- J101 pad 28: /VGA_A10 -> /2_WE#
- J101 pad 29: /VGA_A11 -> /1_WE#
- J101 pad 3: /A2D_0_EN# -> /VGA_A14
- J101 pad 30: /VGA_A12 -> /0_WE#
- J101 pad 31: /VGA_A13 -> /SIGL
- J101 pad 32: /VGA_A14 -> /A2D_0_EN#
- J101 pad 33: /VGA_A15 -> /A2D_2_EN#
- J101 pad 34: /VGA_A16 -> /A2D_1_EN#
- J101 pad 35: /VGA_A17 -> /VGA_A4
- J101 pad 36: /VGA_A18 -> /VGA_A3
- J101 pad 37: /VGA_A19 -> /VGA_A2
- J101 pad 38: /0_OE# -> /VGA_A1
- J101 pad 4: /A2D_1_EN# -> /VGA_A13
- J101 pad 41: /0_WE# -> /VGA_2_A_EN#
- J101 pad 42: /1_OE# -> /VGA_1_A_EN#
- J101 pad 43: /1_WE# -> /VGA_0_A_EN#
- J101 pad 44: /2_OE# -> /VGA_A_L
- J101 pad 45: /2_WE# -> /VGA_A5
- J101 pad 46: /VGA_0_D_EN# -> /VGA_A6
- J101 pad 47: /VGA_1_D_EN# -> /VGA_A15
- J101 pad 48: /VGA_2_D_EN# -> /VGA_A16
- J101 pad 5: /A2D_2_EN# -> /VGA_A12
- J101 pad 51: /A2D_L -> /VGA_A17
- J101 pad 52: /VGA_A_L -> /VGA_A18
- J101 pad 53: /VGA_D_L -> /VGA_A19
- J101 pad 54: unconnected-(J101-Pad54) -> /VGA_A0
- J101 pad 55: unconnected-(J101-Pad55) -> /A2D_L
- J101 pad 6: /BLK_0_EN# -> /VGA_A11
- J101 pad 63: /A2D_X_0 -> /A2D_X7
- J101 pad 64: /A2D_X_1 -> /A2D_X8
- J101 pad 65: /A2D_X_2 -> /A2D_X9
- J101 pad 66: /A2D_X_3 -> /A2D_Y0
- J101 pad 67: /A2D_X_4 -> /A2D_Y1
- J101 pad 68: /A2D_X_5 -> /A2D_Y2
- J101 pad 69: /A2D_X_6 -> /A2D_Y3
- J101 pad 7: /BLK_1_EN# -> /VGA_A10
- J101 pad 70: /A2D_X_7 -> /A2D_Y4
- J101 pad 73: /A2D_X_8 -> /A2D_G0
- J101 pad 74: /A2D_X_9 -> /A2D_G1
- J101 pad 75: /A2D_Y_0 -> /A2D_G2
- J101 pad 76: /A2D_Y_1 -> /A2D_G3
- J101 pad 77: /A2D_Y_2 -> /A2D_R3
- J101 pad 78: /A2D_Y_3 -> /A2D_R2
- J101 pad 79: /A2D_Y_4 -> /A2D_R1
- J101 pad 8: /BLK_2_EN# -> /VGA_A9
- J101 pad 80: /A2D_Y_5 -> /A2D_R0
- J101 pad 83: /A2D_Y_6 -> /A2D_X1
- J101 pad 84: /A2D_Y_7 -> /A2D_X2
- J101 pad 85: /A2D_Y_8 -> /A2D_X3
- J101 pad 86: /A2D_Y_9 -> /A2D_X4
- J101 pad 87: /A2D_B_0 -> /A2D_B0
- J101 pad 88: /A2D_B_1 -> /A2D_B1
- J101 pad 89: /A2D_B_2 -> /A2D_B2
- J101 pad 9: /VGA_0_A_EN# -> /VGA_A8
- J101 pad 90: /A2D_B_3 -> /A2D_B3
- J101 pad 91: /A2D_G_0 -> /A2D_X0
- J101 pad 92: /A2D_G_1 -> /A2D_Y9
- J101 pad 93: /A2D_G_2 -> /A2D_Y8
- J101 pad 94: /A2D_G_3 -> /A2D_Y7
- J101 pad 95: /A2D_R_0 -> /A2D_Y6
- J101 pad 96: /A2D_R_1 -> /A2D_Y5
- J101 pad 97: unconnected-(J101-Pad97) -> /A2D_X6
- J101 pad 98: unconnected-(J101-Pad98) -> /A2D_X5
- J102 pad 10: /A2D_X_7 -> /A2D_Y4
- J102 pad 13: /A2D_X_8 -> /A2D_G0
- J102 pad 14: /A2D_X_9 -> /A2D_G1
- J102 pad 15: /A2D_Y_0 -> /A2D_G2
- J102 pad 16: /A2D_Y_1 -> /A2D_G3
- J102 pad 17: /A2D_Y_2 -> /A2D_R3
- J102 pad 18: /A2D_Y_3 -> /A2D_R2
- J102 pad 19: /A2D_Y_4 -> /A2D_R1
- J102 pad 20: /A2D_Y_5 -> /A2D_R0
- J102 pad 23: /A2D_Y_6 -> /A2D_X1
- J102 pad 24: /A2D_Y_7 -> /A2D_X2
- J102 pad 25: /A2D_Y_8 -> /A2D_X3
- J102 pad 26: /A2D_Y_9 -> /A2D_X4
- J102 pad 27: /A2D_B_0 -> /A2D_B0
- J102 pad 28: /A2D_B_1 -> /A2D_B1
- J102 pad 29: /A2D_B_2 -> /A2D_B2
- J102 pad 3: /A2D_X_0 -> /A2D_X7
- J102 pad 30: /A2D_B_3 -> /A2D_B3
- J102 pad 31: /A2D_G_0 -> /A2D_X0
- J102 pad 32: /A2D_G_1 -> /A2D_Y9
- J102 pad 33: /A2D_G_2 -> /A2D_Y8
- J102 pad 34: /A2D_G_3 -> /A2D_Y7
- J102 pad 35: /A2D_R_0 -> /A2D_Y6
- J102 pad 36: /A2D_R_1 -> /A2D_Y5
- J102 pad 37: /A2D_R_2 -> /A2D_X6
- J102 pad 38: /A2D_R_3 -> /A2D_X5
- J102 pad 4: /A2D_X_1 -> /A2D_X8
- J102 pad 5: /A2D_X_2 -> /A2D_X9
- J102 pad 6: /A2D_X_3 -> /A2D_Y0
- J102 pad 7: /A2D_X_4 -> /A2D_Y1
- J102 pad 8: /A2D_X_5 -> /A2D_Y2
- J102 pad 9: /A2D_X_6 -> /A2D_Y3
- PM101 pad 1: /VGA_R_0 -> /VGA_R0
- PM101 pad 10: /VGA_B_3 -> /VGA_B3
- PM101 pad 2: /VGA_R_1 -> /VGA_R1
- PM101 pad 3: /VGA_R_2 -> /VGA_R2
- PM101 pad 4: /VGA_R_3 -> /VGA_R3
- PM101 pad 7: /VGA_B_0 -> /VGA_B0
- PM101 pad 8: /VGA_B_1 -> /VGA_B1
- PM101 pad 9: /VGA_B_2 -> /VGA_B2
- PM102 pad 1: /VGA_G_0 -> /VGA_G0
- PM102 pad 2: /VGA_G_1 -> /VGA_G1
- PM102 pad 3: /VGA_G_2 -> /VGA_G2
- PM102 pad 4: /VGA_G_3 -> /VGA_G3
- U101 pad 1: /2_A4 -> GND
- U101 pad 10: /2_D2 -> GND
- U101 pad 11: /2_D3 -> /SIGL
- U101 pad 12: +3V3 -> /S_0_WE#
- U101 pad 13: GND -> /S_1_WE#
- U101 pad 14: /2_D4 -> /S_2_WE#
- U101 pad 15: /2_D5 -> /S_0_OE#
- U101 pad 16: /2_D6 -> /S_1_OE#
- U101 pad 17: /2_D7 -> /S_2_OE#
- U101 pad 18: /2_WE# -> /VGA_VSYNC
- U101 pad 19: unconnected-(U101-NC-Pad19) -> /VGA_HSYNC
- U101 pad 2: /2_A3 -> /HSYNC
- U101 pad 20: /2_A19 -> +3V3
- U101 pad 3: /2_A2 -> /VSYNC
- U101 pad 4: /2_A1 -> /2_OE#
- U101 pad 5: /2_A0 -> /1_OE#
- U101 pad 6: unconnected-(U101-NC-Pad6) -> /0_OE#
- U101 pad 7: GND -> /2_WE#
- U101 pad 8: /2_D0 -> /1_WE#
- U101 pad 9: /2_D1 -> /0_WE#
- U102 pad 18: /0_WE# -> /S_0_WE#
- U102 pad 44: /0_OE# -> /S_0_OE#
- U103 pad 18: /1_WE# -> /S_1_WE#
- U103 pad 44: /1_OE# -> /S_1_OE#
- U201 pad 2: /A2D_X_5 -> /A2D_X5
- U201 pad 3: /A2D_X_6 -> /A2D_X6
- U201 pad 4: /A2D_Y_5 -> /A2D_Y5
- U201 pad 5: /A2D_Y_6 -> /A2D_Y6
- U201 pad 6: /A2D_Y_7 -> /A2D_Y7
- U201 pad 7: /A2D_Y_8 -> /A2D_Y8
- U201 pad 8: /A2D_Y_9 -> /A2D_Y9
- U201 pad 9: /A2D_X_0 -> /A2D_X0
- U202 pad 1: /A2D_1_EN# -> /A2D_0_EN#
- U202 pad 12: /1_A0 -> /0_A7
- U202 pad 13: /1_A19 -> /0_A8
- U202 pad 14: /1_A18 -> /0_A9
- U202 pad 15: /1_A17 -> /0_A10
- U202 pad 16: /1_A16 -> /0_A11
- U202 pad 17: /1_A15 -> /0_A12
- U202 pad 18: /1_A6 -> /0_A13
- U202 pad 19: /1_A5 -> /0_A14
- U202 pad 2: /A2D_X_5 -> /A2D_Y4
- U202 pad 3: /A2D_X_6 -> /A2D_Y3
- U202 pad 4: /A2D_Y_5 -> /A2D_Y2
- U202 pad 5: /A2D_Y_6 -> /A2D_Y1
- U202 pad 6: /A2D_Y_7 -> /A2D_Y0
- U202 pad 7: /A2D_Y_8 -> /A2D_X9
- U202 pad 8: /A2D_Y_9 -> /A2D_X8
- U202 pad 9: /A2D_X_0 -> /A2D_X7
- U203 pad 1: /A2D_2_EN# -> /A2D_0_EN#
- U203 pad 12: /2_A0 -> /0_A1
- U203 pad 13: /2_A19 -> /0_A2
- U203 pad 14: /2_A18 -> /0_A3
- U203 pad 15: /2_A17 -> /0_A4
- U203 pad 16: /2_A16 -> /0_D0
- U203 pad 17: /2_A15 -> /0_D1
- U203 pad 18: /2_A6 -> /0_D2
- U203 pad 19: /2_A5 -> /0_D3
- U203 pad 2: /A2D_X_5 -> /A2D_B3
- U203 pad 3: /A2D_X_6 -> /A2D_B2
- U203 pad 4: /A2D_Y_5 -> /A2D_B1
- U203 pad 5: /A2D_Y_6 -> /A2D_B0
- U203 pad 6: /A2D_Y_7 -> /A2D_X4
- U203 pad 7: /A2D_Y_8 -> /A2D_X3
- U203 pad 8: /A2D_Y_9 -> /A2D_X2
- U203 pad 9: /A2D_X_0 -> /A2D_X1
- U204 pad 12: /0_A7 -> /0_D4
- U204 pad 13: /0_A8 -> /0_D5
- U204 pad 14: /0_A9 -> /0_D6
- U204 pad 15: /0_A10 -> /0_D7
- U204 pad 16: /0_A11 -> /0_D11
- U204 pad 17: /0_A12 -> /0_D10
- U204 pad 18: /0_A13 -> /0_D9
- U204 pad 19: /0_A14 -> /0_D8
- U204 pad 2: /A2D_Y_4 -> /A2D_R0
- U204 pad 3: /A2D_Y_3 -> /A2D_R1
- U204 pad 4: /A2D_Y_2 -> /A2D_R2
- U204 pad 5: /A2D_Y_1 -> /A2D_R3
- U204 pad 6: /A2D_Y_0 -> /A2D_G3
- U204 pad 7: /A2D_X_9 -> /A2D_G2
- U204 pad 8: /A2D_X_8 -> /A2D_G1
- U204 pad 9: /A2D_X_7 -> /A2D_G0
- U205 pad 1: /A2D_2_EN# -> /A2D_1_EN#
- U205 pad 12: /2_A7 -> /1_A0
- U205 pad 13: /2_A8 -> /1_A19
- U205 pad 14: /2_A9 -> /1_A18
- U205 pad 15: /2_A10 -> /1_A17
- U205 pad 16: /2_A11 -> /1_A16
- U205 pad 17: /2_A12 -> /1_A15
- U205 pad 18: /2_A13 -> /1_A6
- U205 pad 19: /2_A14 -> /1_A5
- U205 pad 2: /A2D_Y_4 -> /A2D_X5
- U205 pad 3: /A2D_Y_3 -> /A2D_X6
- U205 pad 4: /A2D_Y_2 -> /A2D_Y5
- U205 pad 5: /A2D_Y_1 -> /A2D_Y6
- U205 pad 6: /A2D_Y_0 -> /A2D_Y7
- U205 pad 7: /A2D_X_9 -> /A2D_Y8
- U205 pad 8: /A2D_X_8 -> /A2D_Y9
- U205 pad 9: /A2D_X_7 -> /A2D_X0
- U206 pad 2: /A2D_Y_4 -> /A2D_Y4
- U206 pad 3: /A2D_Y_3 -> /A2D_Y3
- U206 pad 4: /A2D_Y_2 -> /A2D_Y2
- U206 pad 5: /A2D_Y_1 -> /A2D_Y1
- U206 pad 6: /A2D_Y_0 -> /A2D_Y0
- U206 pad 7: /A2D_X_9 -> /A2D_X9
- U206 pad 8: /A2D_X_8 -> /A2D_X8
- U206 pad 9: /A2D_X_7 -> /A2D_X7
- U207 pad 1: /A2D_0_EN# -> /A2D_1_EN#
- U207 pad 12: /0_D0 -> /1_A1
- U207 pad 13: /0_D1 -> /1_A2
- U207 pad 14: /0_D2 -> /1_A3
- U207 pad 15: /0_D3 -> /1_A4
- U207 pad 16: /0_A4 -> /1_D0
- U207 pad 17: /0_A3 -> /1_D1
- U207 pad 18: /0_A2 -> /1_D2
- U207 pad 19: /0_A1 -> /1_D3
- U207 pad 2: /A2D_X_1 -> /A2D_B3
- U207 pad 3: /A2D_X_2 -> /A2D_B2
- U207 pad 4: /A2D_X_3 -> /A2D_B1
- U207 pad 5: /A2D_X_4 -> /A2D_B0
- U207 pad 6: /A2D_B_3 -> /A2D_X4
- U207 pad 7: /A2D_B_2 -> /A2D_X3
- U207 pad 8: /A2D_B_1 -> /A2D_X2
- U207 pad 9: /A2D_B_0 -> /A2D_X1
- U208 pad 1: /A2D_2_EN# -> /A2D_1_EN#
- U208 pad 12: /2_D0 -> /1_D4
- U208 pad 13: /2_D1 -> /1_D5
- U208 pad 14: /2_D2 -> /1_D6
- U208 pad 15: /2_D3 -> /1_D7
- U208 pad 16: /2_A4 -> /1_D11
- U208 pad 17: /2_A3 -> /1_D10
- U208 pad 18: /2_A2 -> /1_D9
- U208 pad 19: /2_A1 -> /1_D8
- U208 pad 2: /A2D_X_1 -> /A2D_R0
- U208 pad 3: /A2D_X_2 -> /A2D_R1
- U208 pad 4: /A2D_X_3 -> /A2D_R2
- U208 pad 5: /A2D_X_4 -> /A2D_R3
- U208 pad 6: /A2D_B_3 -> /A2D_G3
- U208 pad 7: /A2D_B_2 -> /A2D_G2
- U208 pad 8: /A2D_B_1 -> /A2D_G1
- U208 pad 9: /A2D_B_0 -> /A2D_G0
- U209 pad 1: /A2D_1_EN# -> /A2D_2_EN#
- U209 pad 12: /1_D0 -> /2_A0
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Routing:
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- added copper zone on In2.Cu, net +3V3
- added copper zone on B.Cu, net GND
- added copper zone on F.Cu, net GND
- added copper zone on In1.Cu, net GND
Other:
- board size 100 x 100 mm -> 223.2 x 106.5 mm
